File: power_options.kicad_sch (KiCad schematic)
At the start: 15 parts, among them J1 Conn_02x02_Odd_Even, J16 Conn_01x04, J17 Barrel_Jack_Switch, U10 TLV62569DBV

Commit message: more routing
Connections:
- net POE1: now also J1.2 (Pin_2); no longer J1.3 (Pin_3)
- net POE2: now also J1.3 (Pin_3); no longer J1.2 (Pin_2)
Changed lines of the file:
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@@
 	(hierarchical_label "POE1"
+		(shape input)
+		(at 54.61 68.58 0)
+		(effects
+			(font
+				(size 1.27 1.27)
+			)
+			(justify left)
+		)
+	)
+	(hierarchical_label "POE2"
 		(shape input)
 		(at 41.91 66.04 180)
@@
 		)
 	)
-	(hierarchical_label "POE2"
-		(shape input)
-		(at 54.61 68.58 0)
-		(effects
-			(font
-				(size 1.27 1.27)
-			)
-			(justify left)
-		)
-	)

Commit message: clean drc
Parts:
- D8: footprint Diode_SMD:D_0805_2012Metric -> Diode_SMD:D_0603_1608Metric
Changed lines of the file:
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@@
 			)
 		)
-		(property "Footprint" "Diode_SMD:D_0805_2012Metric"
+		(property "Footprint" "Diode_SMD:D_0603_1608Metric"
 			(at 74.93 80.01 90)
 			(hide yes)

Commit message: v1
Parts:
- R26: value 2.2K -> 4.7K
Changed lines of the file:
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@@
 			)
 		)
-		(property "Value" "2.2K"
+		(property "Value" "4.7K"
 			(at 77.47 76.1999 0)
 			(show_name no)

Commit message: Start v2
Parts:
- removed J1: Conn_02x02_Odd_Even, Connector_PinHeader_2.54mm:PinHeader_2x02_P2.54mm_Vertical, symbol Connector_Generic:Conn_02x02_Odd_Even
- removed J16: Conn_01x04, Connector_PinHeader_2.54mm:PinHeader_1x04_P2.54mm_Vertical, symbol Connector_Generic:Conn_01x04
- removed J17: Barrel_Jack_Switch, Connector_BarrelJack:BarrelJack_Horizontal, symbol Connector:Barrel_Jack_Switch
- removed JP2, JP3: Jumper_2_Open, Connector_PinHeader_2.54mm:PinHeader_1x02_P2.54mm_Vertical, symbol Jumper:Jumper_2_Open
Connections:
- no-connect marks 2 -> 0
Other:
- note removed: "2x2 Headers allows us to configure which Mode B pair is GND and which is VDC."
- note removed: "Headers for external wide Vin to 5v like mpm3610 breakout."

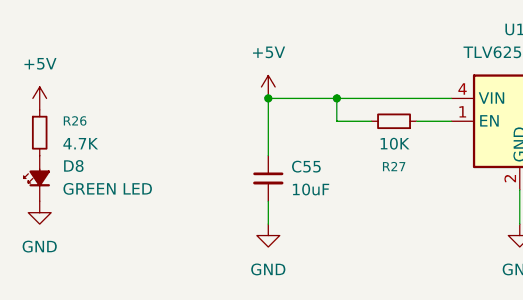
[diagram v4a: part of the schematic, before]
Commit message: Add IO expanders, swap ethernet and move USB LEDs
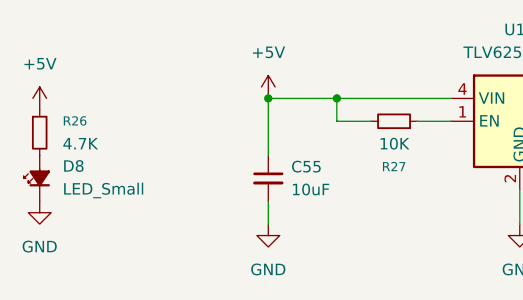
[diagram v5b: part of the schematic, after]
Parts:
- D8: value GREEN LED -> LED_Small; footprint Diode_SMD:D_0603_1608Metric -> LED_SMD:LED_0603_1608Metric
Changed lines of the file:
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@@
 			)
 		)
-		(property "Value" "GREEN LED"
+		(property "Value" "LED_Small"
 			(at 77.47 81.2164 90)
 			(show_name no)
@@
 			)
 		)
-		(property "Footprint" "Diode_SMD:D_0603_1608Metric"
+		(property "Footprint" "LED_SMD:LED_0603_1608Metric"
 			(at 74.93 80.01 90)
 			(hide yes)
